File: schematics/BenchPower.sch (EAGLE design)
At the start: 28 parts, among them U1 V_REG_317SINK, X2 9090-4R

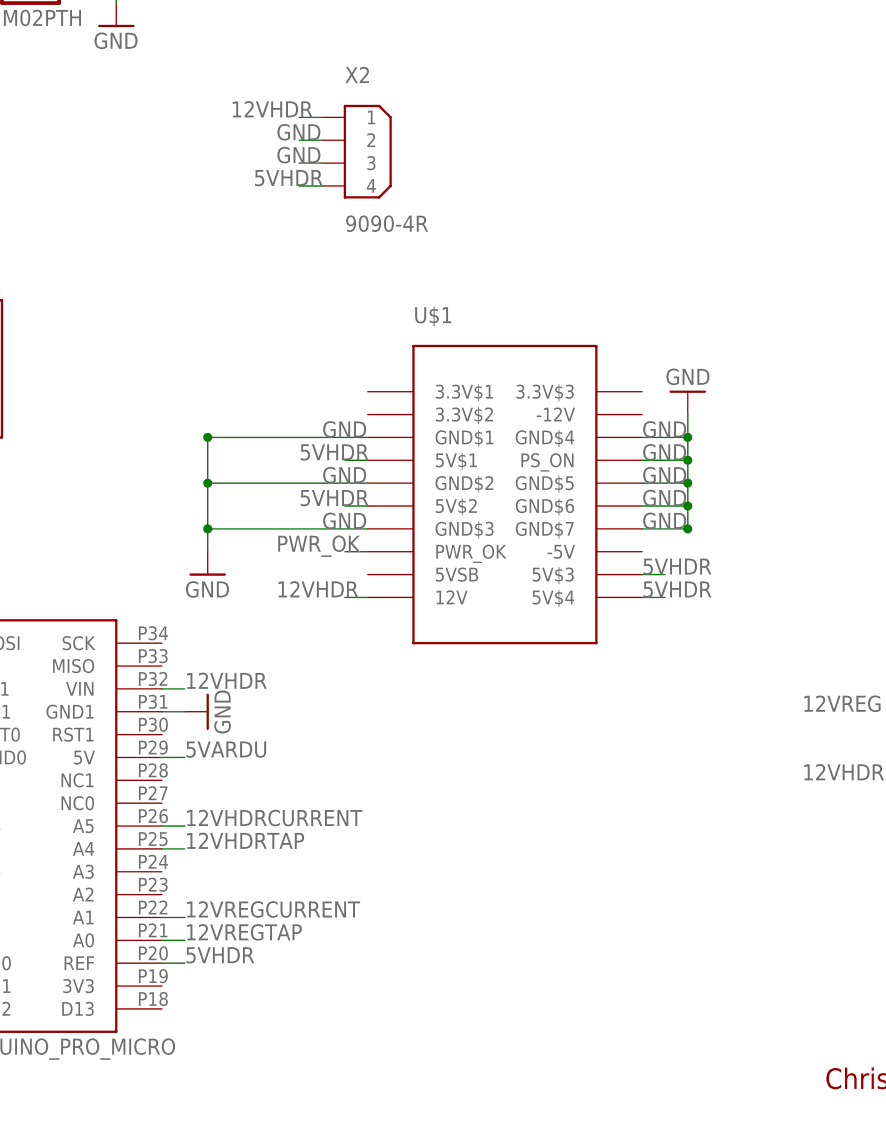
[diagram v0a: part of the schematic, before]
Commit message: Adjust voltage sense software
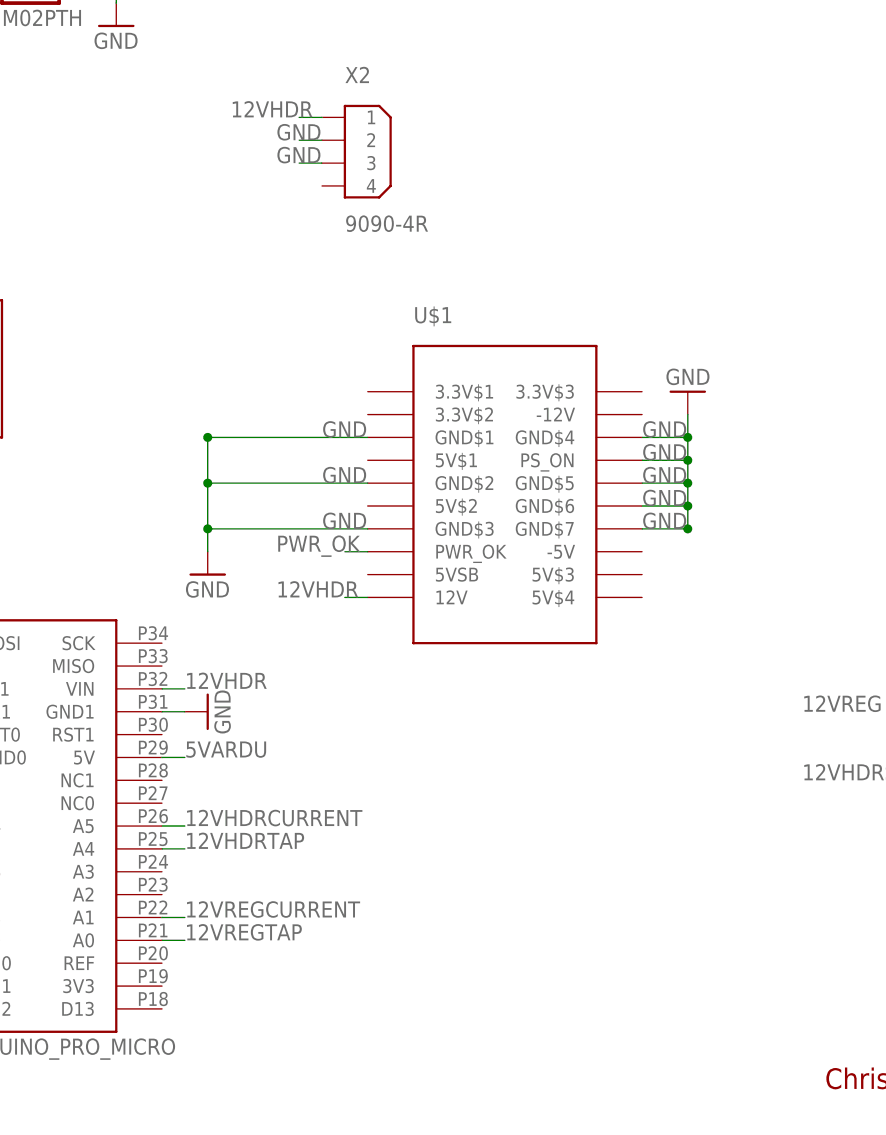
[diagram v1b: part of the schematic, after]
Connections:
- removed net 5VHDR: U$1.5V$1, U$1.5V$2, U$1.5V$3, U$1.5V$4, U$2.REF, X2.4
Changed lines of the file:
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@@
-</segment>
-</net>
-<net name="5VHDR" class="0">
-<segment>
-<pinref part="U$1" gate="G$1" pin="5V$3"/>
-<wire x1="144.78" y1="68.58" x2="147.32" y2="68.58" width="0.1524" layer="91"/>
-<label x="144.78" y="68.58" size="1.778" layer="95"/>
-</segment>
-<segment>
-<pinref part="U$1" gate="G$1" pin="5V$4"/>
-<wire x1="144.78" y1="66.04" x2="147.32" y2="66.04" width="0.1524" layer="91"/>
-<label x="144.78" y="66.04" size="1.778" layer="95"/>
-</segment>
-<segment>
-<pinref part="U$1" gate="G$1" pin="5V$2"/>
-<wire x1="114.3" y1="76.2" x2="111.76" y2="76.2" width="0.1524" layer="91"/>
-<label x="106.68" y="76.2" size="1.778" layer="95"/>
-</segment>
-<segment>
-<pinref part="U$1" gate="G$1" pin="5V$1"/>
-<wire x1="114.3" y1="81.28" x2="111.76" y2="81.28" width="0.1524" layer="91"/>
-<label x="106.68" y="81.28" size="1.778" layer="95"/>
-</segment>
-<segment>
-<pinref part="X2" gate="G$1" pin="4"/>
-<wire x1="109.22" y1="111.76" x2="106.68" y2="111.76" width="0.1524" layer="91"/>
-<label x="101.6" y="111.76" size="1.778" layer="95"/>
-</segment>
-<segment>
-<pinref part="U$2" gate="G$1" pin="REF"/>
-<wire x1="91.44" y1="25.4" x2="93.98" y2="25.4" width="0.1524" layer="91"/>
-<label x="93.98" y="25.4" size="1.778" layer="95"/>
 </segment>
 </net>

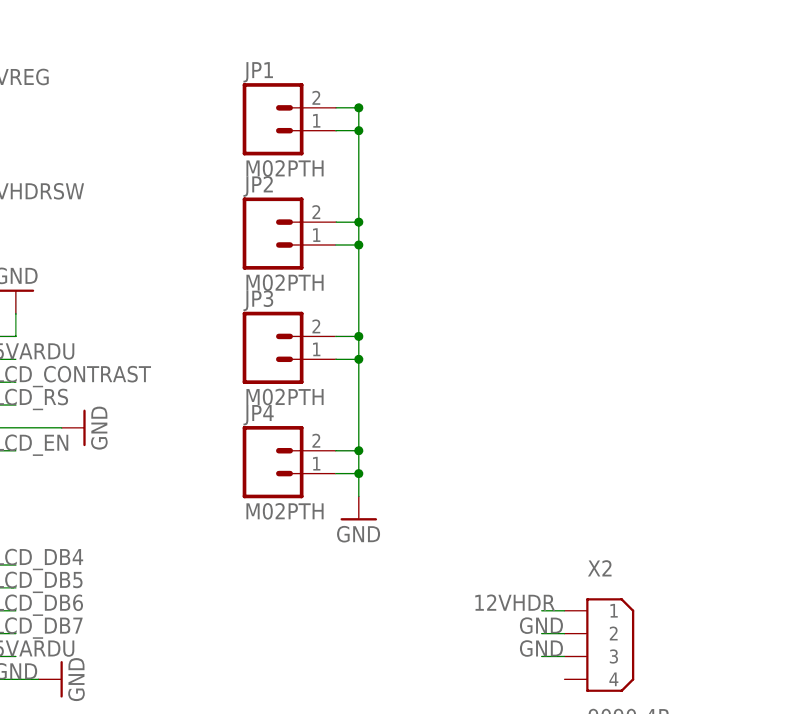
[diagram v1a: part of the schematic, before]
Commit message: Adding new headers for jumper wires
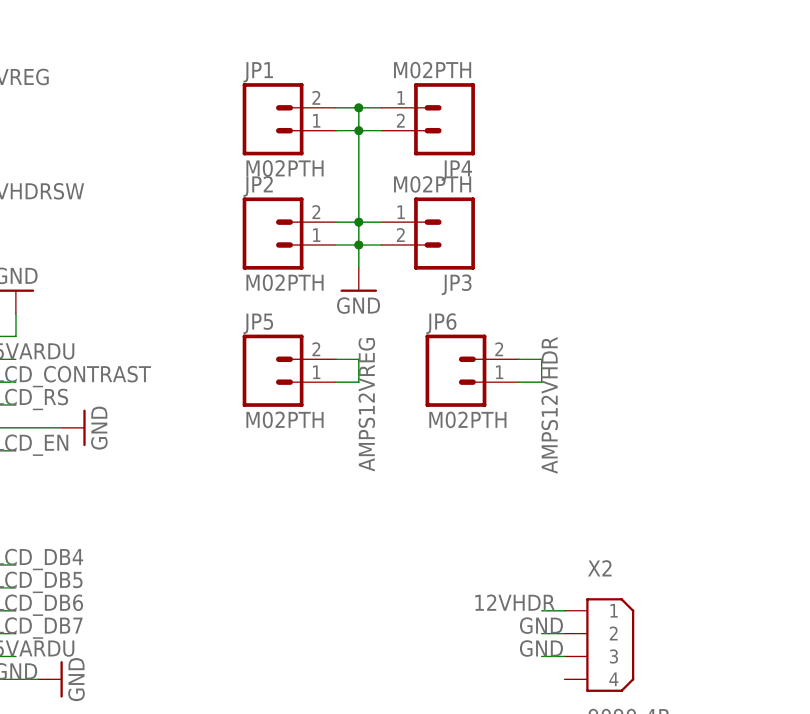
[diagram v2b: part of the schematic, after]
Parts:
- added JP5, JP6: M02PTH, SparkFun-Connectors:M02PTH
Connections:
- net AMPS12VHDR: now also JP6.1, JP6.2
- net AMPS12VREG: now also JP5.1, JP5.2
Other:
- moved on the sheet: JP3, JP4
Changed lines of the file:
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@@
 <?xml version="1.0" encoding="utf-8"?>
 <!DOCTYPE eagle SYSTEM "eagle.dtd">
-<eagle version="6.5.0">
+<eagle version="7.0.0">
 <drawing>
 <settings>
@@
 <part name="GND18" library="SparkFun-Aesthetics" deviceset="GND" device=""/>
 <part name="JP1" library="SparkFun-Connectors" deviceset="M02" device="PTH"/>
-<part name="JP4" library="SparkFun-Connectors" deviceset="M02" device="PTH"/>
 <part name="U5" library="SparkFun-AnalogIC" deviceset="INA139" device=""/>
 <part name="U6" library="SparkFun-AnalogIC" deviceset="INA139" device=""/>
@@
 <part name="S2" library="desjardins" deviceset="EG1213" device=""/>
 <part name="JP2" library="SparkFun-Connectors" deviceset="M02" device="PTH"/>
-<part name="JP3" library="SparkFun-Connectors" deviceset="M02" device="PTH"/>
 <part name="R3" library="SparkFun-Passives" deviceset="RESISTOR" device="AXIAL-0.3" value="100"/>
 <part name="R10" library="SparkFun-Passives" deviceset="RESISTOR" device="AXIAL-0.3" value="140"/>
 <part name="GND3" library="SparkFun-Aesthetics" deviceset="GND" device=""/>
+<part name="JP3" library="SparkFun-Connectors" deviceset="M02" device="PTH"/>
+<part name="JP4" library="SparkFun-Connectors" deviceset="M02" device="PTH"/>
+<part name="JP5" library="SparkFun-Connectors" deviceset="M02" device="PTH"/>
+<part name="JP6" library="SparkFun-Connectors" deviceset="M02" device="PTH"/>
 </parts>
 <sheets>
@@
 <instance part="RV1" gate="G$1" x="30.48" y="50.8" rot="R90"/>
 <instance part="GND17" gate="1" x="17.78" y="50.8" rot="R270"/>
-<instance part="GND18" gate="1" x="86.36" y="129.54"/>
+<instance part="GND18" gate="1" x="86.36" y="154.94"/>
 <instance part="JP1" gate="G$1" x="76.2" y="172.72"/>
-<instance part="JP4" gate="G$1" x="76.2" y="134.62"/>
 <instance part="U5" gate="G$1" x="203.2" y="93.98"/>
 <instance part="U6" gate="G$1" x="203.2" y="154.94"/>
@@
 <instance part="S2" gate="1" x="17.78" y="121.92"/>
 <instance part="JP2" gate="G$1" x="76.2" y="160.02"/>
-<instance part="JP3" gate="G$1" x="76.2" y="147.32"/>
 <instance part="R3" gate="G$1" x="22.86" y="165.1"/>
 <instance part="R10" gate="G$1" x="38.1" y="165.1"/>
 <instance part="GND3" gate="1" x="12.7" y="165.1" rot="R270"/>
+<instance part="JP3" gate="G$1" x="96.52" y="162.56" rot="R180"/>
+<instance part="JP4" gate="G$1" x="96.52" y="175.26" rot="R180"/>
+<instance part="JP5" gate="G$1" x="76.2" y="144.78"/>
+<instance part="JP6" gate="G$1" x="96.52" y="144.78"/>
 </instances>
 <busses>
@@
 <wire x1="86.36" y1="172.72" x2="86.36" y2="162.56" width="0.1524" layer="91"/>
 <wire x1="86.36" y1="162.56" x2="86.36" y2="160.02" width="0.1524" layer="91"/>
-<wire x1="86.36" y1="160.02" x2="86.36" y2="149.86" width="0.1524" layer="91"/>
-<wire x1="86.36" y1="149.86" x2="86.36" y2="147.32" width="0.1524" layer="91"/>
-<wire x1="86.36" y1="147.32" x2="86.36" y2="137.16" width="0.1524" layer="91"/>
-<wire x1="86.36" y1="137.16" x2="86.36" y2="134.62" width="0.1524" layer="91"/>
-<wire x1="86.36" y1="134.62" x2="86.36" y2="132.08" width="0.1524" layer="91"/>
+<wire x1="86.36" y1="160.02" x2="86.36" y2="157.48" width="0.1524" layer="91"/>
 <wire x1="83.82" y1="172.72" x2="86.36" y2="172.72" width="0.1524" layer="91"/>
+<junction x="86.36" y="172.72"/>
+<pinref part="JP4" gate="G$1" pin="1"/>
+<wire x1="88.9" y1="175.26" x2="86.36" y2="175.26" width="0.1524" layer="91"/>
+<pinref part="JP4" gate="G$1" pin="2"/>
+<wire x1="88.9" y1="172.72" x2="86.36" y2="172.72" width="0.1524" layer="91"/>
+<pinref part="JP3" gate="G$1" pin="1"/>
+<wire x1="88.9" y1="162.56" x2="86.36" y2="162.56" width="0.1524" layer="91"/>
+<pinref part="JP3" gate="G$1" pin="2"/>
+<wire x1="88.9" y1="160.02" x2="86.36" y2="160.02" width="0.1524" layer="91"/>
+<pinref part="JP2" gate="G$1" pin="1"/>
+<wire x1="83.82" y1="160.02" x2="86.36" y2="160.02" width="0.1524" layer="91"/>
 <pinref part="JP2" gate="G$1" pin="2"/>
 <wire x1="83.82" y1="162.56" x2="86.36" y2="162.56" width="0.1524" layer="91"/>
-<pinref part="JP2" gate="G$1" pin="1"/>
-<wire x1="83.82" y1="160.02" x2="86.36" y2="160.02" width="0.1524" layer="91"/>
-<pinref part="JP3" gate="G$1" pin="2"/>
-<wire x1="83.82" y1="149.86" x2="86.36" y2="149.86" width="0.1524" layer="91"/>
-<pinref part="JP3" gate="G$1" pin="1"/>
-<wire x1="83.82" y1="147.32" x2="86.36" y2="147.32" width="0.1524" layer="91"/>
-<pinref part="JP4" gate="G$1" pin="2"/>
-<wire x1="83.82" y1="137.16" x2="86.36" y2="137.16" width="0.1524" layer="91"/>
-<pinref part="JP4" gate="G$1" pin="1"/>
-<wire x1="83.82" y1="134.62" x2="86.36" y2="134.62" width="0.1524" layer="91"/>
-<junction x="86.36" y="134.62"/>
-<junction x="86.36" y="137.16"/>
-<junction x="86.36" y="147.32"/>
-<junction x="86.36" y="149.86"/>
 <junction x="86.36" y="160.02"/>
 <junction x="86.36" y="162.56"/>
-<junction x="86.36" y="172.72"/>
 <junction x="86.36" y="175.26"/>
 </segment>
@@
 <label x="210.82" y="167.64" size="1.778" layer="95" rot="R90"/>
 </segment>
+<segment>
+<pinref part="JP5" gate="G$1" pin="2"/>
+<wire x1="83.82" y1="147.32" x2="86.36" y2="147.32" width="0.1524" layer="91"/>
+<wire x1="86.36" y1="147.32" x2="86.36" y2="144.78" width="0.1524" layer="91"/>
+<pinref part="JP5" gate="G$1" pin="1"/>
+<wire x1="83.82" y1="144.78" x2="86.36" y2="144.78" width="0.1524" layer="91"/>
+<label x="86.36" y="149.86" size="1.778" layer="95" rot="R270"/>
+</segment>
 </net>
 <net name="AMPS12VHDR" class="0">
@@
 <label x="210.82" y="106.68" size="1.778" layer="95" rot="R90"/>
 </segment>
-</net>
+<segment>
+<pinref part="JP6" gate="G$1" pin="2"/>
+<wire x1="104.14" y1="147.32" x2="106.68" y2="147.32" width="0.1524" layer="91"/>
+<wire x1="106.68" y1="147.32" x2="106.68" y2="144.78" width="0.1524" layer="91"/>
+<pinref part="JP6" gate="G$1" pin="1"/>
+<wire x1="104.14" y1="144.78" x2="106.68" y2="144.78" width="0.1524" layer="91"/>
+<label x="106.68" y="149.86" size="1.778" layer="95" rot="R270"/>
+</segment>
+</net>

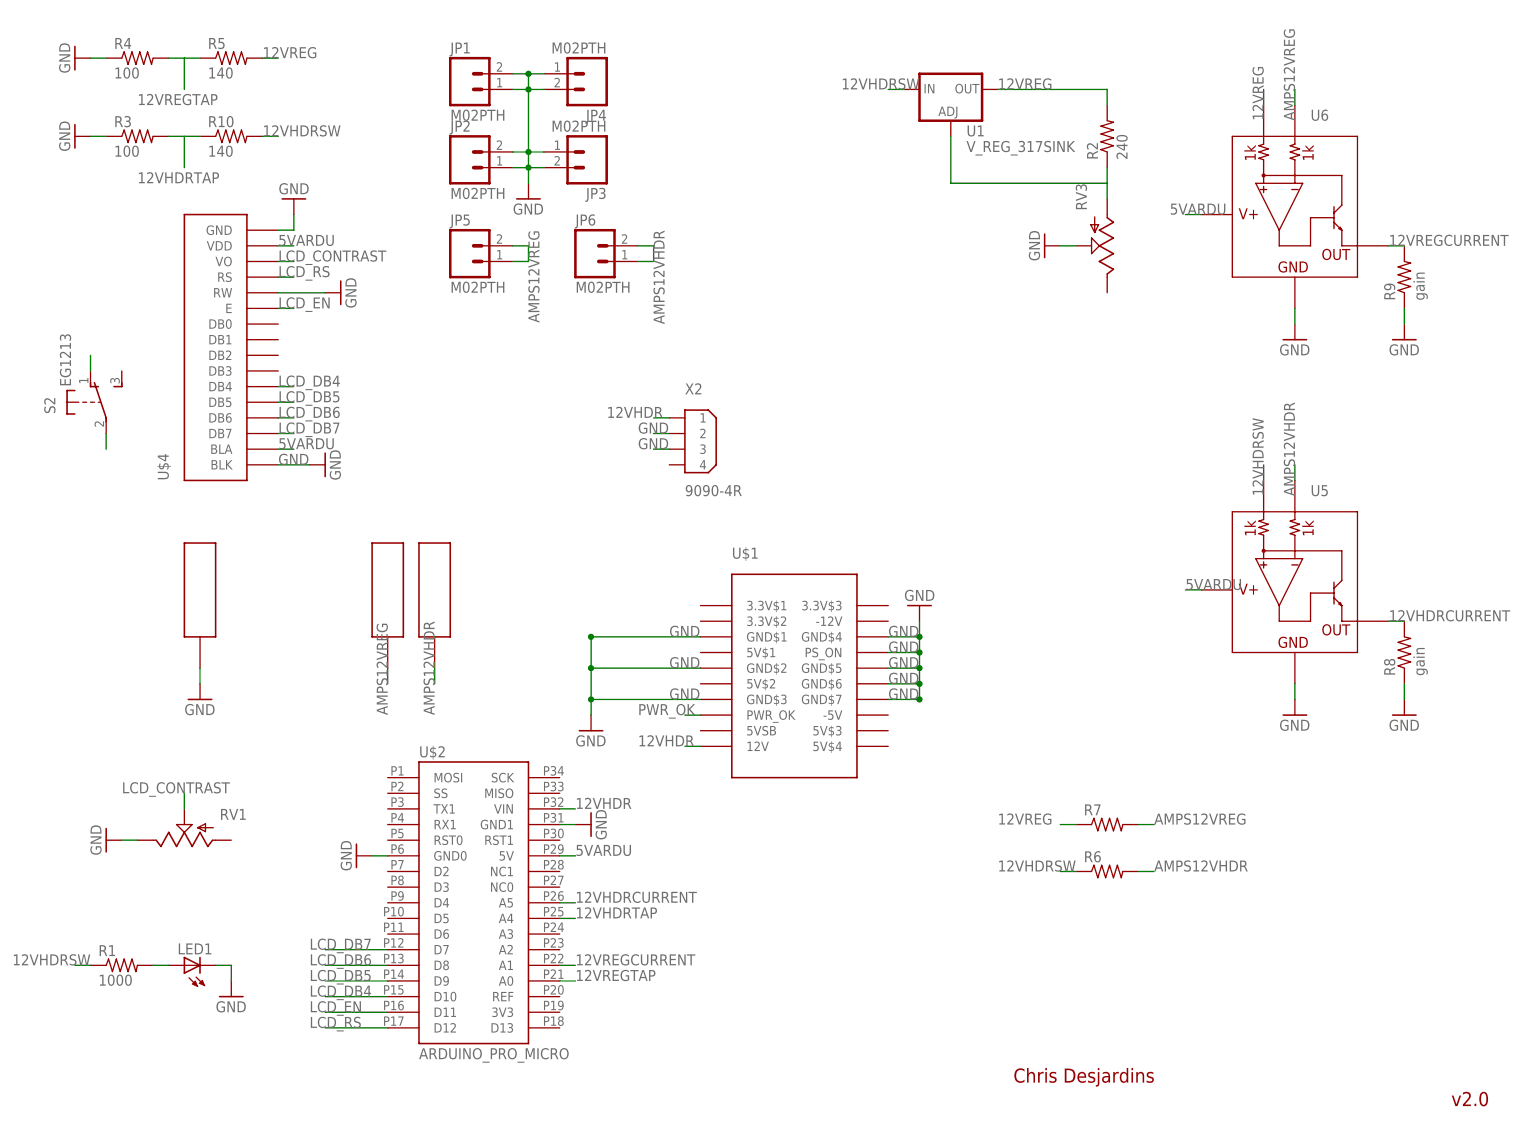
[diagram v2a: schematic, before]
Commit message: Move pot off board, and other updates for v2.0
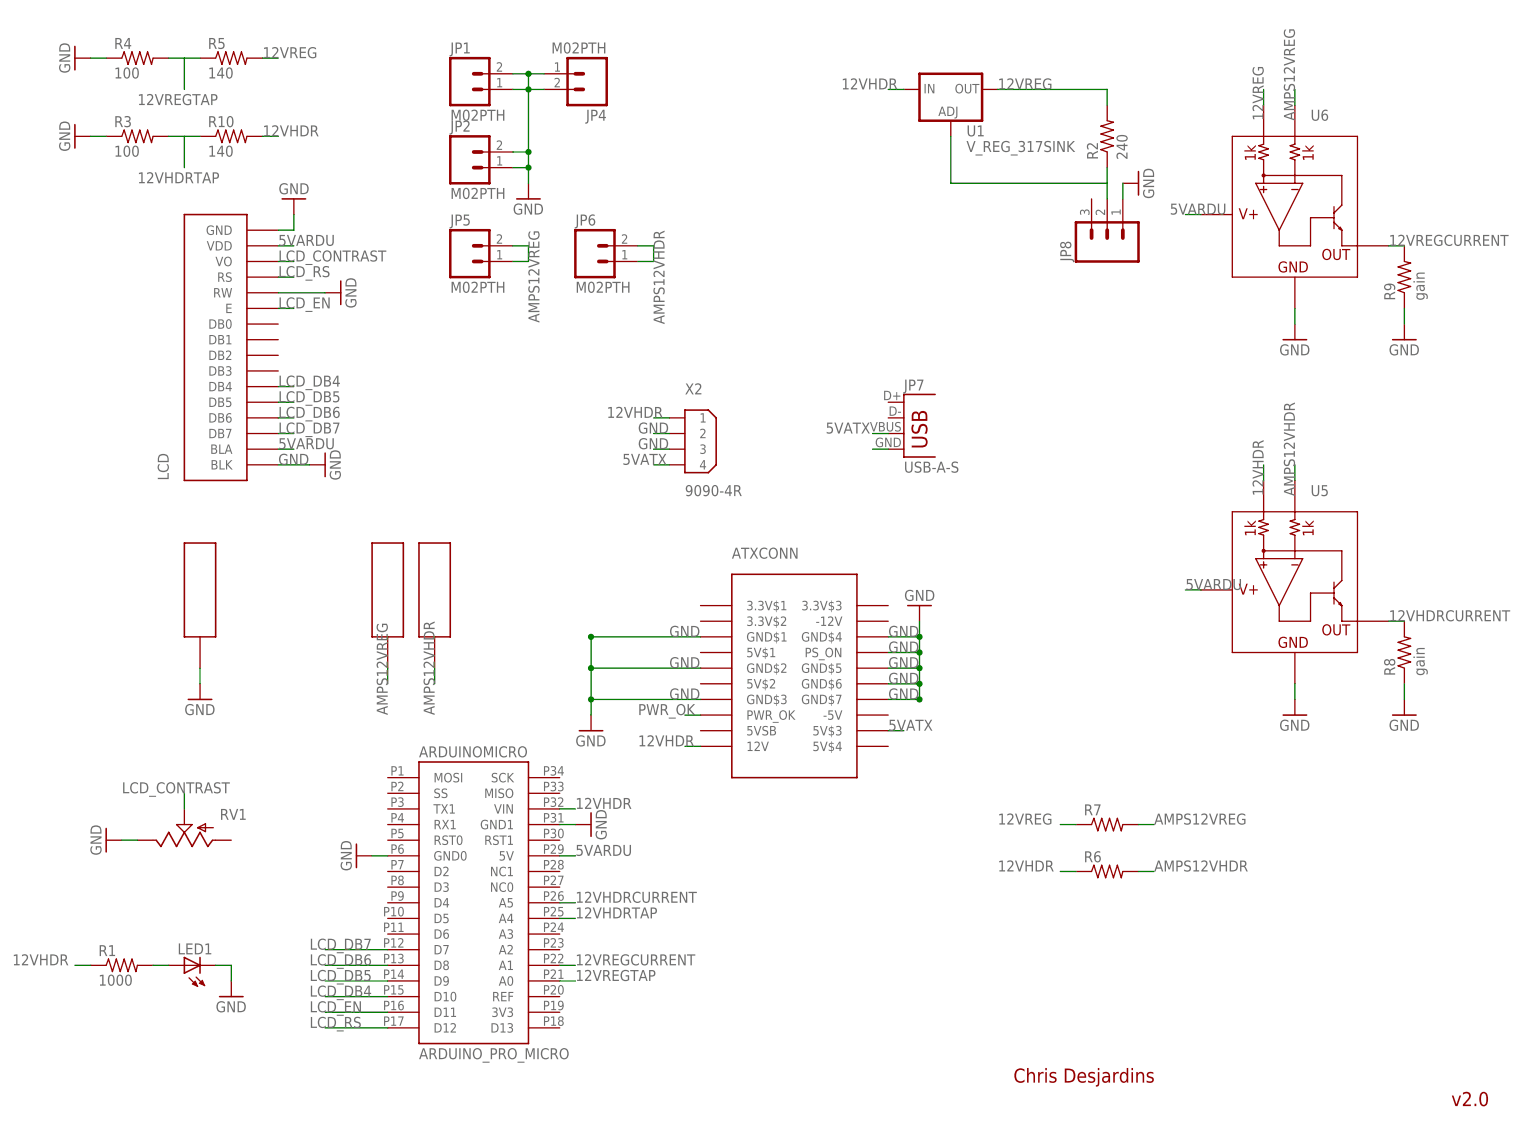
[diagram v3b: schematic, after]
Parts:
- removed JP3: M02PTH, SparkFun-Connectors:M02PTH
- removed RV3: (no value), desjardins:POT
- removed S2: EG1213, desjardins:EG1213
- added JP7: USB-A-S, SparkFun-Connectors:USB-A-S
- added JP8: (no value), SparkFun-Connectors:M03PTH
- renumbered U$1 to ATXCONN, U$2 to ARDUINOMICRO, U$4 to LCD
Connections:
- removed net 12VHDRSW: R1.1, R10.2, R6.1, S2.P, U1.IN, U5.VIN+
- new net 5VATX: ATXCONN.5V$3, JP7.VBUS, X2.4
- net 12VHDR: now also R1.1, R10.2, R6.1, U1.IN, U5.VIN+; no longer S2.O
- net ADJREG1: now also JP8.2; no longer RV3.A
- net GND: now also JP7.GND, JP8.1; no longer JP3.1, JP3.2, RV3.S
